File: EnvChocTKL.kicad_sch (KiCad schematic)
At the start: 185 parts, among them U1 EliteC

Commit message: converted MCU from elite-c to onboard RP2040
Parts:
- removed U1: EliteC, Keebio-Parts:Elite-C, symbol keebio:Elite-C
- added C1: 10uf 402, Capacitor_SMD:C_0402_1005Metric, symbol Device:C
- added C10, C3: 1uf 0201, Capacitor_SMD:C_0201_0603Metric, symbol Device:C
- added C11, C13, C14, C15, C16, C18, C5, C6, C7, C8: 100nf 0201, Capacitor_SMD:C_0201_0603Metric, symbol Device:C
- added C17, C4, CBP1: 10uf 0402, Capacitor_SMD:C_0402_1005Metric, symbol Device:C
- added C19, C2: 22pf 0402, Capacitor_SMD:C_0402_1005Metric, symbol Device:C
- added D1: 1N4002W, Diode_SMD:D_SOD-123, symbol Device:D_Schottky
- added F1: 0805L050WR, Fuse:Fuse_0805_2012Metric, symbol Device:Polyfuse_Small
- added FB1: FerriteBead, Resistor_SMD:R_0402_1005Metric, symbol Device:FerriteBead_Small
- added FLASH1: W25Q16JVUXIQ, Package_SON:SON-8-1EP_3x2mm_P0.5mm_EP1.4x1.6mm, symbol W25Q256JVEIQ_TR:W25Q256JVEIQ_TR
- added GPIO24_LED1, GPIO25_LED1: LED_0402, LED_SMD:LED_0402_1005Metric, symbol Device:LED
- added GPIO24_RESISTOR1, GPIO25_RESISTOR1: 470 0402 Resistor, Resistor_SMD:R_0402_1005Metric, symbol Device:R
- added J2, RSW1: SKRKAEE020, Button_Switch_SMD:SW_Push_SPST_NO_Alps_SKRK, symbol Switch:SW_Push
- added J5: Conn_01x03_Male, Connector_PinHeader_2.54mm:PinHeader_1x03_P2.54mm_Vertical, symbol Connector_Generic:Conn_01x03
- added NT1: NetTie_2, NetTie:NetTie-2_SMD_Pad0.5mm, symbol Device:NetTie_2
- added Q1: Si2329DS, Package_TO_SOT_SMD:SOT-23, symbol Transistor_FET:Si2319CDS
- added R1, R11: 1K 0201, Capacitor_SMD:C_0201_0603Metric, symbol Device:R
- added R10: 1 0402, Resistor_SMD:R_0402_1005Metric, symbol Device:R_Small
- added R2: 10K 0201, Capacitor_SMD:C_0201_0603Metric, symbol Device:R
- added R3, R4: 27 0402 Resistor, Resistor_SMD:R_0402_1005Metric, symbol Device:R
- added R5, R6: 5.1K 0402, Resistor_SMD:R_0402_1005Metric, symbol Device:R_Small
- added R7: 100K 0402 resistor, Resistor_SMD:R_0402_1005Metric, symbol Device:R
- added R9: 200 0603, Resistor_SMD:R_0603_1608Metric, symbol Device:R_Small
- added U1: TLV75533PDBVR, Package_TO_SOT_SMD:SOT-23-5, symbol Regulator_Linear:AP131-15
- added U3: RP2040, RP2040_minimal:RP2040-QFN-56, symbol MCU_RaspberryPi_RP2040:RP2040
- added USB1: TYPE-C-31-M-12, HRO-TYPE-C31-M-12:HRO-TYPE-C-31-M-12, symbol Type-C:HRO-TYPE-C-31-M-12
- added Y1: 3225_4P, Crystal:Crystal_SMD_3225-4Pin_3.2x2.5mm, symbol Device:Crystal_GND24
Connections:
- net GND: now also C1.2, C10.2, C11.2, C13.2, C14.2, C15.2, C16.2, C17.2, C18.2, C19.1, C2.1, C3.2, C4.2, C5.2, C6.2, C7.2, C8.2, CBP1.2, FLASH1.4 (GND), FLASH1.9 (EXP), GPIO24_LED1.1 (K), GPIO25_LED1.1 (K), J2.2, J5.2 (Pin_2), NT1.1, R5.1, R6.1, RSW1.1, U1.2 (GND), U3.19 (TESTEN), U3.57 (GND), USB1.1 (GND), USB1.12 (GND), USB1.13 (SHIELD), Y1.2, Y1.4
- net col0: now also U3.8 (GPIO6)
- net col1: now also U3.9 (GPIO7)
- net col10: now also U3.27 (GPIO16)
- net col11: now also U3.28 (GPIO17)
- net col12: now also U3.29 (GPIO18)
- net col13: now also U3.30 (GPIO19)
- net col14: now also U3.31 (GPIO20)
- net col15: now also U3.32 (GPIO21)
- net col16: now also U3.34 (GPIO22)
- net col17: now also U3.35 (GPIO23)
- net col2: now also U3.11 (GPIO8)
- net col3: now also U3.12 (GPIO9)
- net col4: now also U3.13 (GPIO10)
- net col5: now also U3.14 (GPIO11)
- net col6: now also U3.15 (GPIO12)
- net col7: now also U3.16 (GPIO13)
- net col8: now also U3.17 (GPIO14)
- net col9: now also U3.18 (GPIO15)
- net row0: now also U3.36 (GPIO24)
- net row1: now also U3.37 (GPIO25)
- net row2: now also U3.38 (GPIO26_ADC0)
- net row3: now also U3.39 (GPIO27_ADC1)
- net row4: now also U3.40 (GPIO28_ADC2)
- net row5: now also U3.41 (GPIO29_ADC3)
- new net: R4.2, U3.46 (USB_DM)
- new net: R3.2, U3.47 (USB_DP)
- new net: R6.2, USB1.10 (CC2)
- new net: R5.2, USB1.4 (CC1)
- new net: C1.1, FB1.2, U1.1 (IN)
- new net: GPIO25_LED1.2 (A), GPIO25_RESISTOR1.1
- new net: C19.2, R11.2, Y1.3
- new net: CBP1.1, U1.4 (BP)
- new net: GPIO24_RESISTOR1.2, Q1.3 (D)
- new net: GPIO24_LED1.2 (A), GPIO24_RESISTOR1.1
- new net: F1.1, FB1.1
- new net +1V1: C3.1, C6.1, C7.1, U3.23 (DVDD), U3.45 (VREG_VOUT), U3.50 (DVDD)
- new net +3V3: C10.1, C11.1, C13.1, C14.1, C15.1, C16.1, C17.1, C18.1, C4.1, C5.1, C8.1, FLASH1.8 (VCC), Q1.2 (S), R10.2, R2.1, R9.1, U1.5 (OUT), U3.1 (IOVDD), U3.10 (IOVDD), U3.22 (IOVDD), U3.33 (IOVDD), U3.42 (IOVDD), U3.43 (ADC_AVDD), U3.44 (VREG_IN), U3.48 (USB_VDD), U3.49 (IOVDD)
- new net 3V3_EN: R7.1, U1.3 (EN)
- new net ADC_VREF: R10.1, R9.2
- new net AGND: NT1.2
- new net GPIO0: GPIO25_RESISTOR1.2, U3.2 (GPIO0)
- new net GPIO1: Q1.1 (G), U3.3 (GPIO1)
- new net GPIO2: U3.4 (GPIO2)
- new net GPIO3: U3.5 (GPIO3)
- new net GPIO4: U3.6 (GPIO4)
- new net GPIO5: U3.7 (GPIO5)
- new net QSPI_SCLK: FLASH1.6 (CLK), U3.52 (QSPI_SCLK)
- new net QSPI_SD0: FLASH1.5 (DI(IO0)), U3.53 (QSPI_SD0)
- new net QSPI_SD1: FLASH1.2 (DO(IO1)), U3.55 (QSPI_SD1)
- new net QSPI_SD2: FLASH1.3 (IO2), U3.54 (QSPI_SD2)
- new net QSPI_SD3: FLASH1.7 (IO3), U3.51 (QSPI_SD3)
- new net QSPI_SS: FLASH1.1 (~{CS}), R1.1, R2.2, U3.56 (QSPI_SS)
- new net RUN: RSW1.2, U3.26 (RUN)
- new net SWCLK: J5.1 (Pin_1), U3.24 (SWCLK)
- new net SWD: J5.3 (Pin_3), U3.25 (SWD)
- new net USB_D+: R3.1, USB1.6 (DP1), USB1.8 (DP2)
- new net USB_D-: R4.1, USB1.5 (DN2), USB1.7 (DN1)
- new net VBUS: D1.2 (A), R7.2, USB1.11 (VBUS), USB1.2 (VBUS)
- new net VSYS: D1.1 (K), F1.2
- new net XIN: C2.2, U3.20 (XIN), Y1.1
- new net XOUT: R11.1, U3.21 (XOUT)
- new net ~{USB_BOOT}: J2.1, R1.2
- no-connect marks 0 -> 2
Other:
- note added: "1K resistor to prevent overdriving of the crystal as per the minimal design example"
- note added: "2x 5.1K Resistors on the CC pins will = 5V@1.5A this is the recomended default config for type-c"
- note added: "500mA hold current 1A trip 6V trip"
- note added: "Crystal"
- note added: "D1 NEEDS to be 0omh resistor or 1N4002 diode"
- note added: "Flash"
- note added: "GD25Q40CEIGR is NOT Compatible you need GD25W16* needs to be a multiple of 8 atleast for circuitpython. (Ive not confirmed if GD25W16 works I just Have some boards with GD25Q40CEIGR and they dont work)"
- note added: "GPIOs"
- note added: "Im pretty sure a lot of these W25QXXX Chips are pin compatible Dont quote me on that"
- note added: "Im unsure if the RP2040 can function with flash larger than 128Mb"
- note added: "KoreanHROParts USB_C_Receptacle_HRO_TYPE-C-31-M-12"
- note added: "LEDs"
- note added: "MAKE SURE THIS LINE is ran off of pin43 or close to pin43"
- note added: "Make sure C10 is close to pin 44 of RP2040"
- note added: "Make sure C3 is close to pin 45 of RP2040"
- note added: "Make sure R3 and R4 are close to RP2040"
- note added: "Make sure the flash chip you have selected supports 3.3V power or adjust the design."
- note added: "Only fit cBP1 if you have selected an alternate voltage regulator TLV75533PDBVR does not require cBP1."
- note added: "Pin 9 technically doesnt exist its the main central contact under the chip for heat dicipation"
- note added: "Power LED is on by default but when GPIO24 is enabled it will be shut off"
- note added: "RP2040 supports 1MHz to 15MHz"
- note added: "These decoupling capacitors are meant to be put close by each 3.3V pin of the RP2040"
- note added: "USB/POWER"
- note added: "Would assume you could just not connect SD2 and SD3 for non QSPI"
- note added: "https://datasheets.raspberrypi.com/rp2040/hardware-design-with-rp2040.pdf On page 13 you can learn more details of what flash is supported"
- note added: "not 22pf but pick to match crystal."
- note added: "suposedly the rp2040 supports SPI-2 flash but I havent tried it."
- note added: "this is for factory testing always pull this to ground"
- moved on the sheet: D_0, D_1, D_10, D_11, D_12, D_13, D_14, D_15, D_16, D_17, D_18, D_19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

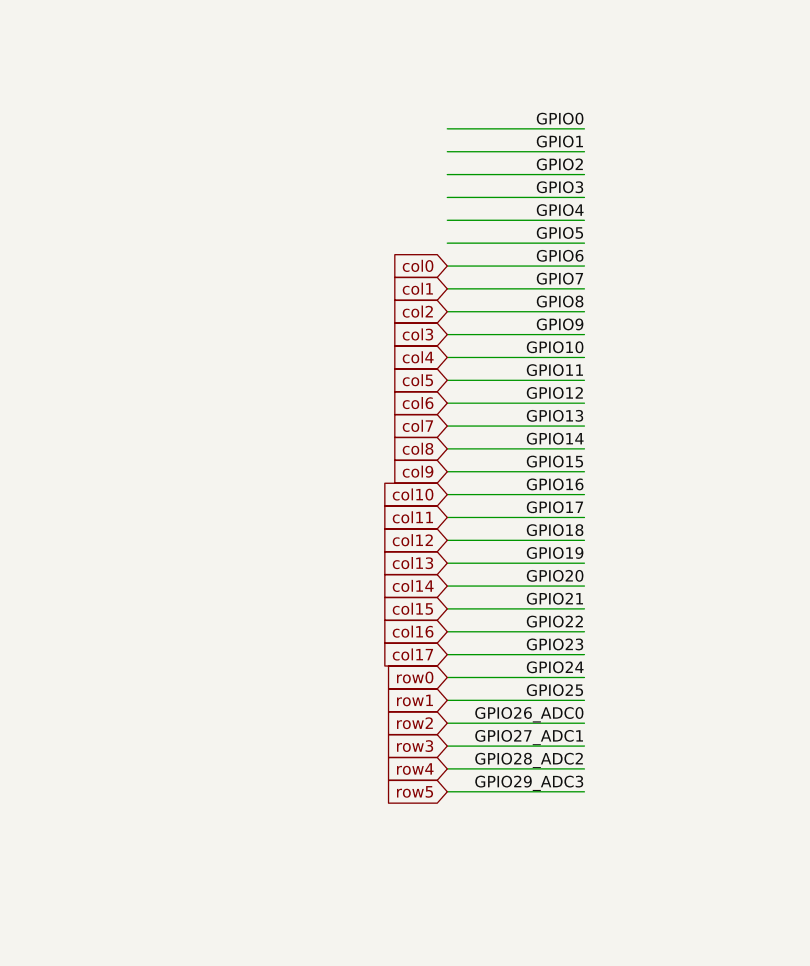
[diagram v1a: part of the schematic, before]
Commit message: flipped MCU to other side
might optimize the space usage of the MCU so I can have a more normal top row.
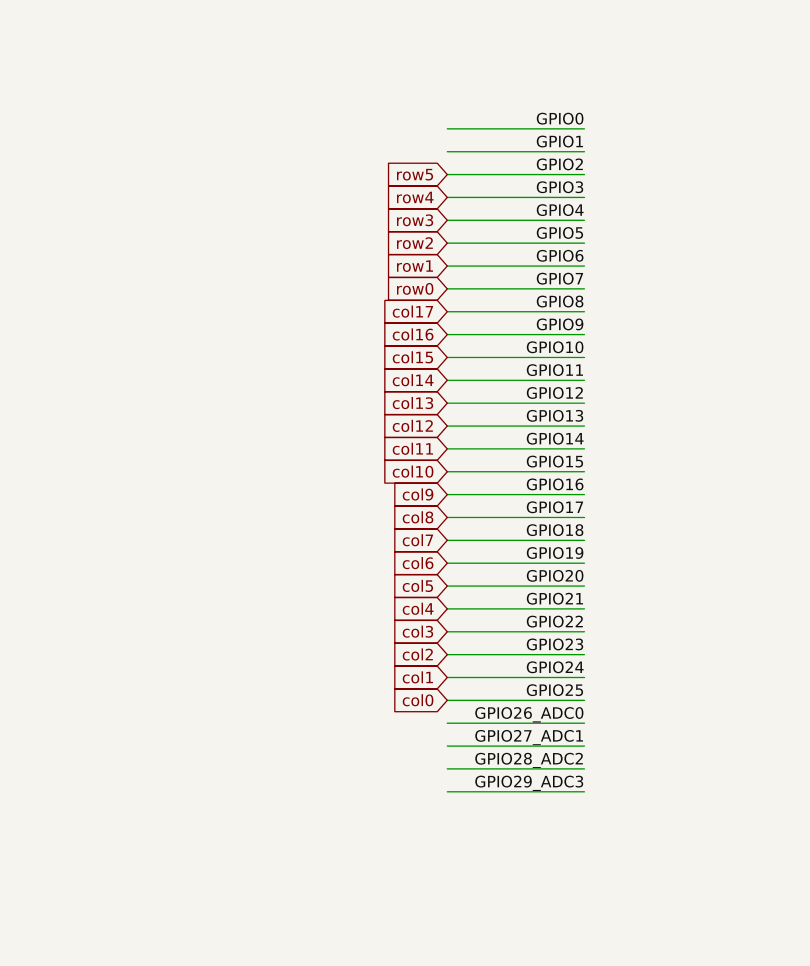
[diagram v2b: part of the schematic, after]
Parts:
- J5: footprint Connector_PinHeader_2.54mm:PinHeader_1x03_P2.54mm_Vertical -> Connector_JST:JST_PH_B3B-PH-SM4-TB_1x03-1MP_P2.00mm_Vertical
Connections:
- net GPIO2 is gone; now on net row5: U3.4 (GPIO2)
- net GPIO3 is gone; now on net row4: U3.5 (GPIO3)
- net GPIO4 is gone; now on net row3: U3.6 (GPIO4)
- net GPIO5 is gone; now on net row2: U3.7 (GPIO5)
- net col0: now also U3.37 (GPIO25); no longer U3.8 (GPIO6)
- net col1: now also U3.36 (GPIO24); no longer U3.9 (GPIO7)
- net col10: now also U3.18 (GPIO15); no longer U3.27 (GPIO16)
- net col11: now also U3.17 (GPIO14); no longer U3.28 (GPIO17)
- net col12: now also U3.16 (GPIO13); no longer U3.29 (GPIO18)
- net col13: now also U3.15 (GPIO12); no longer U3.30 (GPIO19)
- net col14: now also U3.14 (GPIO11); no longer U3.31 (GPIO20)
- net col15: now also U3.13 (GPIO10); no longer U3.32 (GPIO21)
- net col16: now also U3.12 (GPIO9); no longer U3.34 (GPIO22)
- net col17: now also U3.11 (GPIO8); no longer U3.35 (GPIO23)
- net col2: now also U3.35 (GPIO23); no longer U3.11 (GPIO8)
- net col3: now also U3.34 (GPIO22); no longer U3.12 (GPIO9)
- net col4: now also U3.32 (GPIO21); no longer U3.13 (GPIO10)
- net col5: now also U3.31 (GPIO20); no longer U3.14 (GPIO11)
- net col6: now also U3.30 (GPIO19); no longer U3.15 (GPIO12)
- net col7: now also U3.29 (GPIO18); no longer U3.16 (GPIO13)
- net col8: now also U3.28 (GPIO17); no longer U3.17 (GPIO14)
- net col9: now also U3.27 (GPIO16); no longer U3.18 (GPIO15)
- net row0: now also U3.9 (GPIO7); no longer U3.36 (GPIO24)
- net row1: now also U3.8 (GPIO6); no longer U3.37 (GPIO25)
- net row2: no longer U3.38 (GPIO26_ADC0)
- net row3: no longer U3.39 (GPIO27_ADC1)
- net row4: no longer U3.40 (GPIO28_ADC2)
- net row5: no longer U3.41 (GPIO29_ADC3)
- new net GPIO26_ADC0: U3.38 (GPIO26_ADC0)
- new net GPIO27_ADC1: U3.39 (GPIO27_ADC1)
- new net GPIO28_ADC2: U3.40 (GPIO28_ADC2)
- new net GPIO29_ADC3: U3.41 (GPIO29_ADC3)

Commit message: generated updated Gerbers and made appropriate part changes
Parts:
- FLASH1: value W25Q16JVUXIQ -> W25Q16J
- R1, R11: footprint Capacitor_SMD:C_0201_0603Metric -> Resistor_SMD:R_0201_0603Metric
- R2: value 10K 0201 -> 10K 0402; footprint Capacitor_SMD:C_0201_0603Metric -> Resistor_SMD:R_0402_1005Metric
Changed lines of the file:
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@@
       (effects (font (size 1.27 1.27)) (justify left))
     )
-    (property "Value" "10K 0201" (id 1) (at 65.278 111.633 0)
-      (effects (font (size 1.27 1.27)) (justify left))
-    )
-    (property "Footprint" "Capacitor_SMD:C_0201_0603Metric" (id 2) (at 61.722 110.49 90)
+    (property "Value" "10K 0402" (id 1) (at 65.278 111.633 0)
+      (effects (font (size 1.27 1.27)) (justify left))
+    )
+    (property "Footprint" "Resistor_SMD:R_0402_1005Metric" (id 2) (at 61.722 110.49 90)
       (effects (font (size 1.27 1.27)) hide)
     )
@@
     (property "Reference" "R1" (id 0) (at 48.26 120.4722 90))
     (property "Value" "1K 0201" (id 1) (at 48.26 122.7836 90))
-    (property "Footprint" "Capacitor_SMD:C_0201_0603Metric" (id 2) (at 48.26 123.952 90)
+    (property "Footprint" "Resistor_SMD:R_0201_0603Metric" (id 2) (at 48.26 123.952 90)
       (effects (font (size 1.27 1.27)) hide)
     )
@@
     (in_bom yes) (on_board yes)
     (property "Reference" "FLASH1" (id 0) (at 78.74 133.35 0))
-    (property "Value" "W25Q16JVUXIQ" (id 1) (at 78.74 146.05 0))
+    (property "Value" "W25Q16J" (id 1) (at 78.74 146.05 0))
     (property "Footprint" "Package_SON:SON-8-1EP_3x2mm_P0.5mm_EP1.4x1.6mm" (id 2) (at 78.74 133.35 0)
       (effects (font (size 1.27 1.27)) (justify left bottom) hide)
@@
     (property "Reference" "R11" (id 0) (at 69.85 203.0222 90))
     (property "Value" "1K 0201" (id 1) (at 69.85 205.3336 90))
-    (property "Footprint" "Capacitor_SMD:C_0201_0603Metric" (id 2) (at 69.85 206.502 90)
+    (property "Footprint" "Resistor_SMD:R_0201_0603Metric" (id 2) (at 69.85 206.502 90)
       (effects (font (size 1.27 1.27)) hide)
     )
@@
     )
     (path "/00000000-0000-0000-0000-0000608edada"
-      (reference "FLASH1") (unit 1) (value "W25Q16JVUXIQ") (footprint "Package_SON:SON-8-1EP_3x2mm_P0.5mm_EP1.4x1.6mm")
+      (reference "FLASH1") (unit 1) (value "W25Q16J") (footprint "Package_SON:SON-8-1EP_3x2mm_P0.5mm_EP1.4x1.6mm")
     )
     (path "/00000000-0000-0000-0000-000061cdafdc"
@@
     )
     (path "/00000000-0000-0000-0000-00005edae9f0"
-      (reference "R1") (unit 1) (value "1K 0201") (footprint "Capacitor_SMD:C_0201_0603Metric")
+      (reference "R1") (unit 1) (value "1K 0201") (footprint "Resistor_SMD:R_0201_0603Metric")
     )
     (path "/00000000-0000-0000-0000-00005edac067"
-      (reference "R2") (unit 1) (value "10K 0201") (footprint "Capacitor_SMD:C_0201_0603Metric")
+      (reference "R2") (unit 1) (value "10K 0402") (footprint "Resistor_SMD:R_0402_1005Metric")
     )
     (path "/00000000-0000-0000-0000-00005ede0881"
@@
     )
     (path "/00000000-0000-0000-0000-00006150e6ab"
-      (reference "R11") (unit 1) (value "1K 0201") (footprint "Capacitor_SMD:C_0201_0603Metric")
+      (reference "R11") (unit 1) (value "1K 0201") (footprint "Resistor_SMD:R_0201_0603Metric")
     )
     (path "/00000000-0000-0000-0000-00006142c001"

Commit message: swapped flash for lager SOIC-8 and removed some parts.
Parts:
- FLASH1: value W25Q16J -> W25Q16JVSSIQ; footprint Package_SON:SON-8-1EP_3x2mm_P0.5mm_EP1.4x1.6mm -> Package_SO:SOIC-8_5.23x5.23mm_P1.27mm
- J5: footprint Connector_JST:JST_PH_B3B-PH-SM4-TB_1x03-1MP_P2.00mm_Vertical -> TestPoint:TestPoint_2Pads_Pitch2.54mm_Drill0.8mm
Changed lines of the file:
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@@
     (in_bom yes) (on_board yes)
     (property "Reference" "FLASH1" (id 0) (at 78.74 133.35 0))
-    (property "Value" "W25Q16J" (id 1) (at 78.74 146.05 0))
-    (property "Footprint" "Package_SON:SON-8-1EP_3x2mm_P0.5mm_EP1.4x1.6mm" (id 2) (at 78.74 133.35 0)
+    (property "Value" "W25Q16JVSSIQ" (id 1) (at 78.74 146.05 0))
+    (property "Footprint" "Package_SO:SOIC-8_5.23x5.23mm_P1.27mm" (id 2) (at 78.74 133.35 0)
       (effects (font (size 1.27 1.27)) (justify left bottom) hide)
     )
@@
       (effects (font (size 1.27 1.27)) (justify left))
     )
-    (property "Footprint" "Connector_JST:JST_PH_B3B-PH-SM4-TB_1x03-1MP_P2.00mm_Vertical" (id 2) (at 299.72 118.11 0)
+    (property "Footprint" "TestPoint:TestPoint_2Pads_Pitch2.54mm_Drill0.8mm" (id 2) (at 299.72 118.11 0)
       (effects (font (size 1.27 1.27)) hide)
     )
@@
     )
     (path "/00000000-0000-0000-0000-0000608edada"
-      (reference "FLASH1") (unit 1) (value "W25Q16J") (footprint "Package_SON:SON-8-1EP_3x2mm_P0.5mm_EP1.4x1.6mm")
+      (reference "FLASH1") (unit 1) (value "W25Q16JVSSIQ") (footprint "Package_SO:SOIC-8_5.23x5.23mm_P1.27mm")
     )
     (path "/00000000-0000-0000-0000-000061cdafdc"
@@
     )
     (path "/00000000-0000-0000-0000-000060ce2dd4"
-      (reference "J5") (unit 1) (value "Conn_01x03_Male") (footprint "Connector_JST:JST_PH_B3B-PH-SM4-TB_1x03-1MP_P2.00mm_Vertical")
+      (reference "J5") (unit 1) (value "Conn_01x03_Male") (footprint "TestPoint:TestPoint_2Pads_Pitch2.54mm_Drill0.8mm")
     )
     (path "/00000000-0000-0000-0000-000000000001"

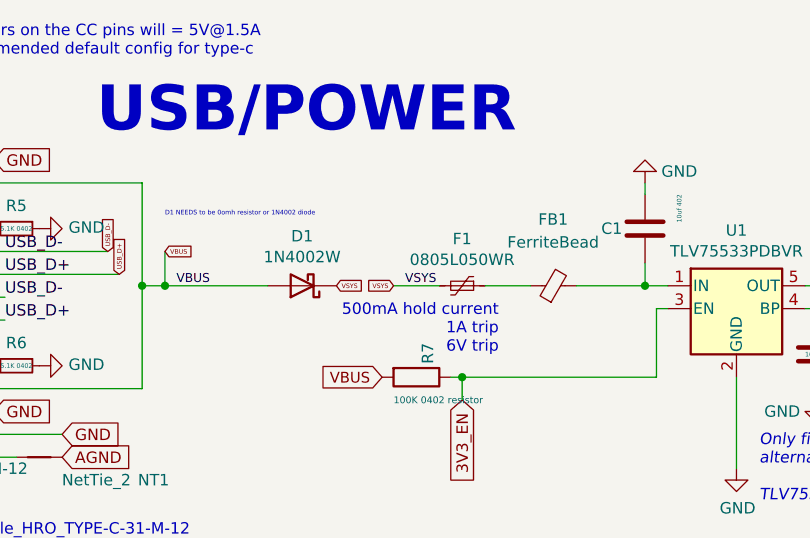
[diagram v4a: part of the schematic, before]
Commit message: IMPORTANT FIX
for some reason a lot of the switches were slightly misaligned to MX spacing and also added cutouts for Choc stabs on Eco.User to be exported as DXF for whatever.
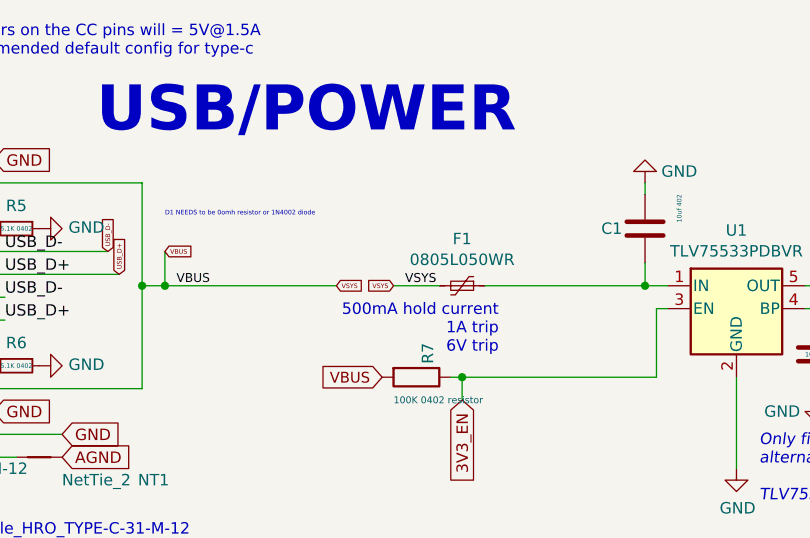
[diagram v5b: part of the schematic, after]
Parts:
- removed D1: 1N4002W, Diode_SMD:D_SOD-123, symbol Device:D_Schottky
- removed FB1: FerriteBead, Resistor_SMD:R_0402_1005Metric, symbol Device:FerriteBead_Small
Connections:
- net VSYS is gone; now on net VBUS: F1.2
- net at C1.1, U1.1 (IN): now also F1.1
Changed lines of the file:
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@@
     (stroke (width 0) (type default) (color 0 0 0 0))
   )
-  (wire (pts (xy 92.71 44.45) (xy 100.33 44.45))
-    (stroke (width 0) (type default) (color 0 0 0 0))
-  )
   (wire (pts (xy 229.87 162.56) (xy 245.11 162.56))
     (stroke (width 0) (type default) (color 0 0 0 0))
@@
     (stroke (width 0) (type default) (color 0 0 0 0))
   )
-  (wire (pts (xy 46.99 44.45) (xy 58.42 44.45))
+  (wire (pts (xy 46.99 44.45) (xy 66.04 44.45))
     (stroke (width 0) (type default) (color 0 0 0 0))
   )
@@
     (stroke (width 0) (type default) (color 0 0 0 0))
   )
-  (wire (pts (xy 82.55 44.45) (xy 87.63 44.45))
+  (wire (pts (xy 82.55 44.45) (xy 100.33 44.45))
     (stroke (width 0) (type default) (color 0 0 0 0))
   )
@@
     (pin "1")
   )
-  (symbol (lib_id "Device:D_Schottky") (at 62.23 44.45 180) (unit 1)
-    (in_bom yes) (on_board yes)
-    (property "Reference" "D1" (id 0) (at 62.23 38.9382 0))
-    (property "Value" "1N4002W" (id 1) (at 62.23 41.2496 0))
-    (property "Footprint" "Diode_SMD:D_SOD-123" (id 2) (at 62.23 44.45 0)
-      (effects (font (size 1.27 1.27)) hide)
-    )
-    (property "Datasheet" "" (id 3) (at 62.23 44.45 0)
-      (effects (font (size 1.27 1.27)) hide)
-    )
-    (property "LCSC" " " (id 4) (at 62.23 44.45 0)
-      (effects (font (size 1.27 1.27)) hide)
-    )
-    (pin "1")
-    (pin "2")
-  )
   (symbol (lib_id "Device:C") (at 138.43 48.26 0) (unit 1)
     (in_bom yes) (on_board yes)
@@
     (pin "2")
   )
-  (symbol (lib_id "Device:FerriteBead_Small") (at 90.17 44.45 90) (unit 1)
-    (in_bom yes) (on_board yes) (fields_autoplaced)
-    (property "Reference" "FB1" (id 0) (at 90.1192 37.084 90))
-    (property "Value" "FerriteBead" (id 1) (at 90.1192 39.624 90))
-    (property "Footprint" "Resistor_SMD:R_0402_1005Metric" (id 2) (at 90.17 46.228 90)
-      (effects (font (size 1.27 1.27)) hide)
-    )
-    (property "Datasheet" "~" (id 3) (at 90.17 44.45 0)
-      (effects (font (size 1.27 1.27)) hide)
-    )
-    (pin "1")
-    (pin "2")
-  )
   (symbol (lib_id "Device:D_Small") (at 64.77 240.03 90) (unit 1)
     (in_bom yes) (on_board yes)
@@
       (reference "CBP1") (unit 1) (value "10uf 0402") (footprint "Capacitor_SMD:C_0402_1005Metric")
     )
-    (path "/00000000-0000-0000-0000-000061068f6f"
-      (reference "D1") (unit 1) (value "1N4002W") (footprint "Diode_SMD:D_SOD-123")
-    )
     (path "/fa7799b8-da0f-4085-bfe8-a8838b0e9e0b"
       (reference "D_0") (unit 1) (value "D") (footprint "Diode_SMD:D_SOD-123")
@@
       (reference "F1") (unit 1) (value "0805L050WR") (footprint "Fuse:Fuse_0805_2012Metric")
     )
-    (path "/cb658bfb-bb44-442b-af68-cdf8168ed728"
-      (reference "FB1") (unit 1) (value "FerriteBead") (footprint "Resistor_SMD:R_0402_1005Metric")
-    )
     (path "/00000000-0000-0000-0000-0000608edada"
